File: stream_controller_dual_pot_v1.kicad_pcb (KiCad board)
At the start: 2 copper layers, 46.5 x 48 mm, 36 parts, among them Q1 Q_PMOS_GDS, Q2 Q_PMOS_GDS, SW1 SW_SPDT, U1 MCP1825S, U2 MCP2221AxSL, U3 MCP73831-2-OT, U5 ESP32_WROVER_E, U6 MIC803

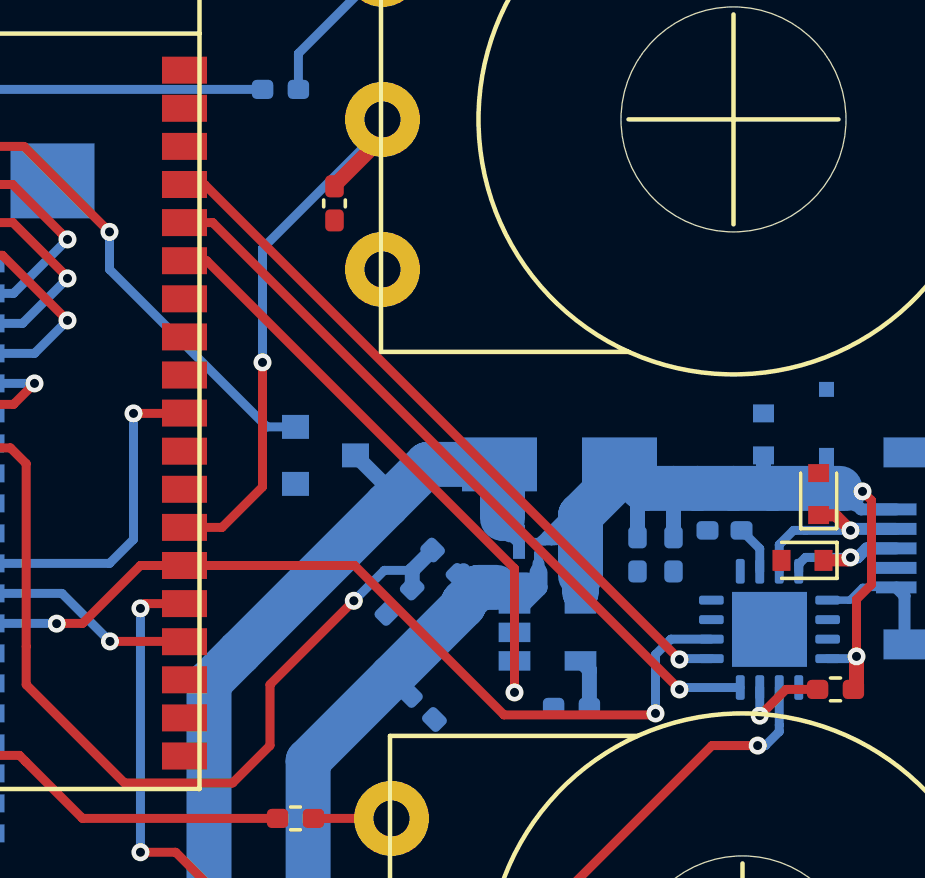
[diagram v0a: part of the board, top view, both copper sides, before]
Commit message: bug UART corrigé
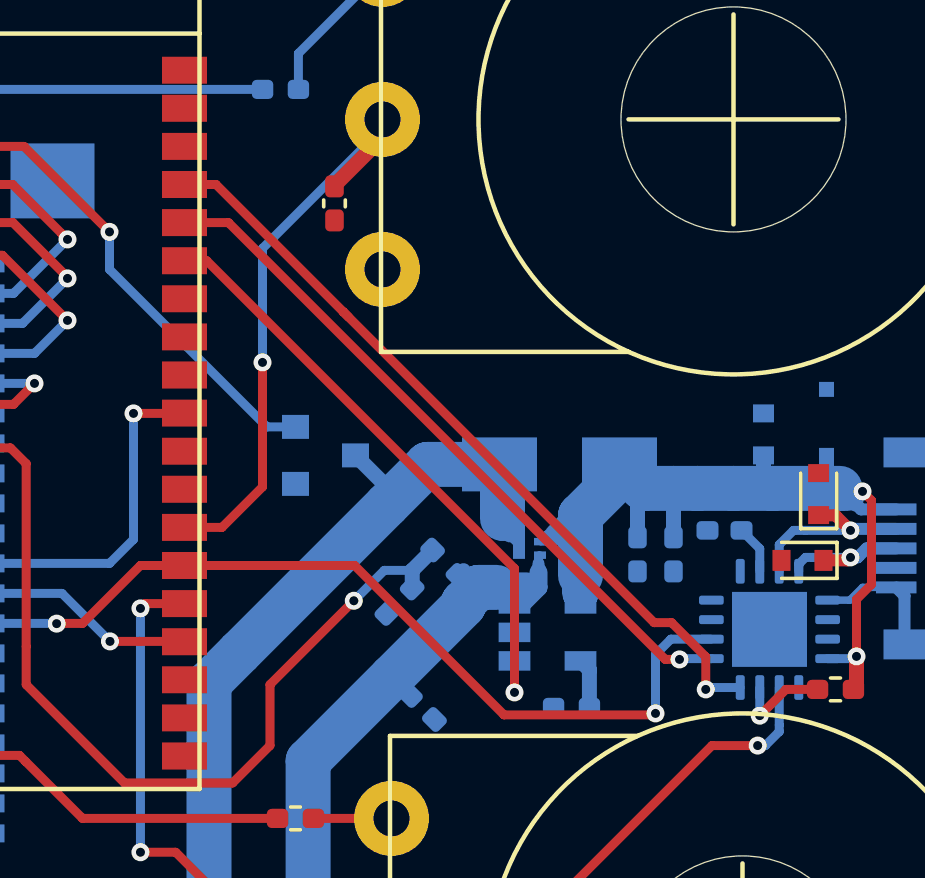
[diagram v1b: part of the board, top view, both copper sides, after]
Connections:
- U2 pad 4: RXD0 -> TXD0
- U2 pad 5: TXD0 -> RXD0
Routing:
- net TXD0: track 24.1 -> 27.1 mm
- net RXD0: track 25.0 -> 23.6 mm

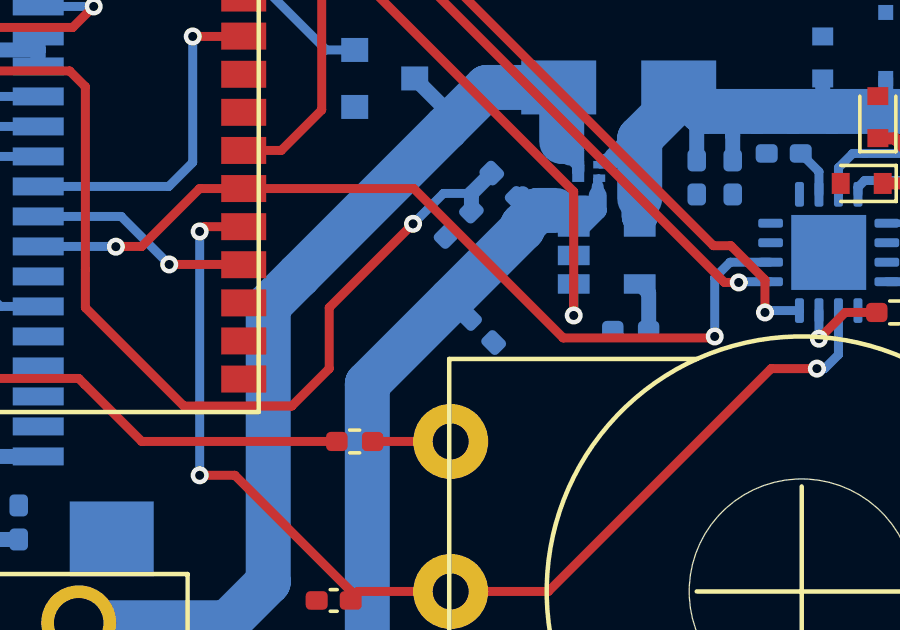
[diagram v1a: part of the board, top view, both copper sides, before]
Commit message: Correction IO0 forcé à 1
Si IO0 n'est pas haut au démarrage, l'ESP32 se met en mode flash. Quand non-connecté par USB, IO0 doit être forcé à 1, car le contrôleur USB n'est pas alimenté.
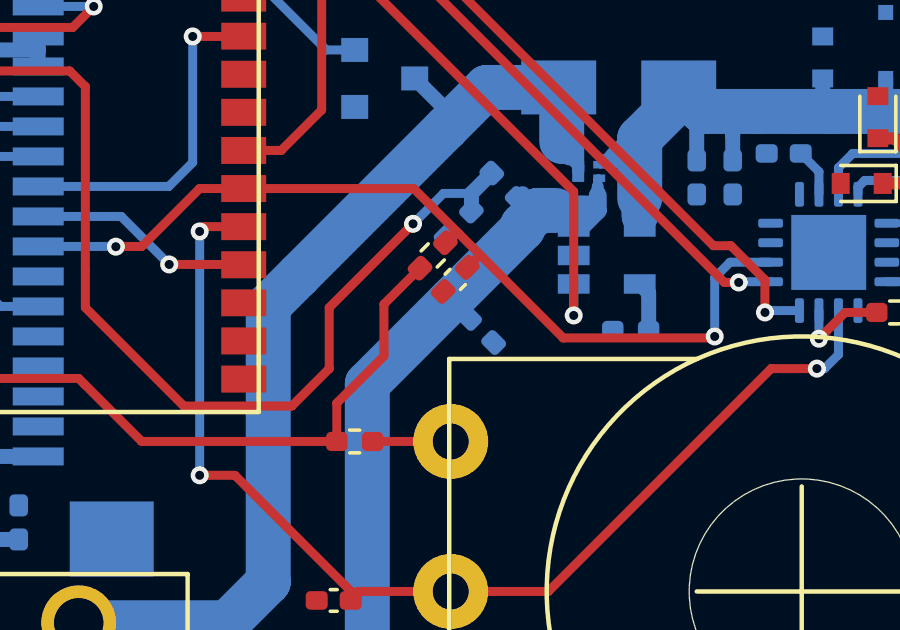
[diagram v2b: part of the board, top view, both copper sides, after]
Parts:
- added C10: 100nF 25V, Capacitor_SMD:C_0402_1005Metric_Pad0.74x0.62mm_HandSolder, F.Cu at (68.0, 33.6)
- added R8: 10k 5%, Resistor_SMD:R_0402_1005Metric_Pad0.72x0.64mm_HandSolder, F.Cu at (67.2, 32.8)
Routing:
- net 3V3: track 88.7 -> 95.6 mm
- net FLASH: track 29.5 -> 30.7 mm

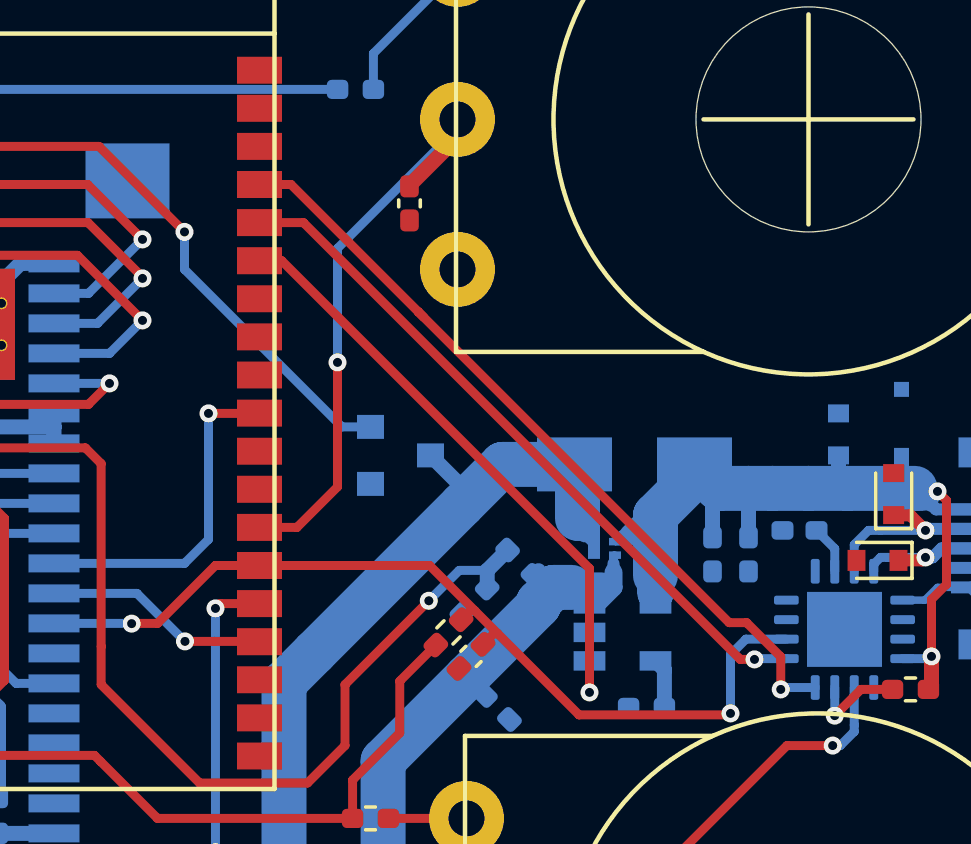
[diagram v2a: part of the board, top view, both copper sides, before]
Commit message: Ajout contrôle pin EN par contrôleur USB
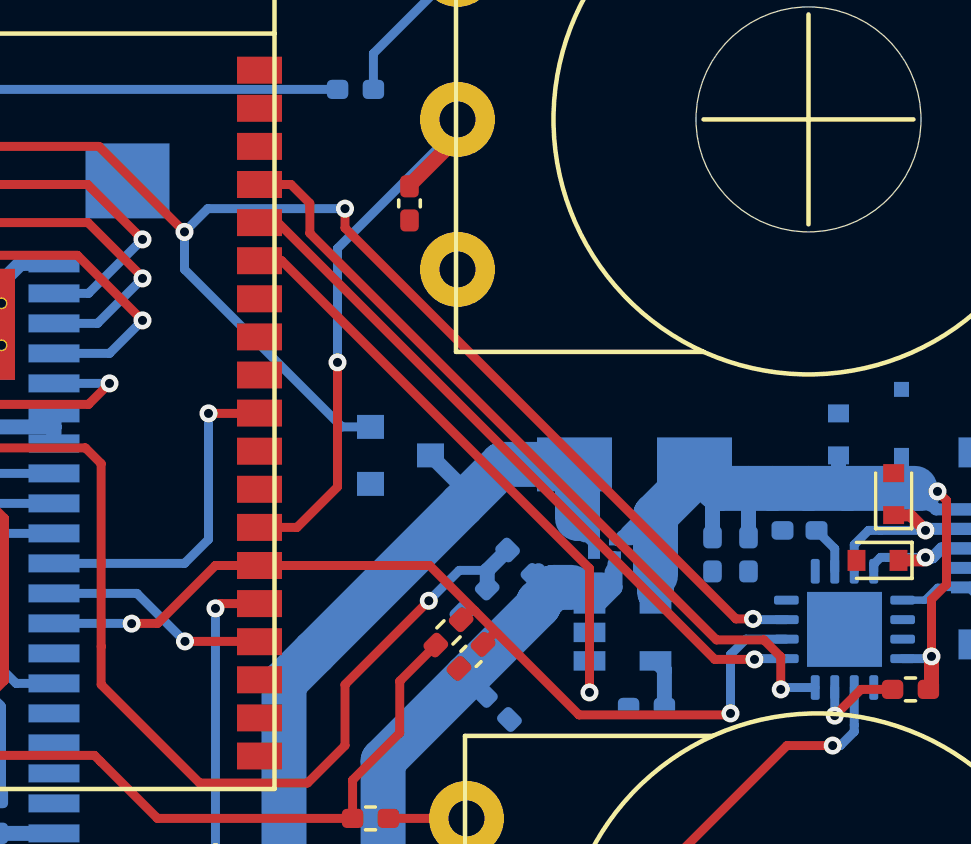
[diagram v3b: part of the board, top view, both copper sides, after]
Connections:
- U2 pad 7: (no net) -> EN
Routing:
- net EN: track 26.0 -> 52.5 mm, vias 2 -> 4
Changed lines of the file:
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@@
     (thickness 1.6)
     (drawings 59)
-    (tracks 394)
+    (tracks 403)
     (zones 0)
     (modules 38)
@@
     (add_net "Net-(D2-Pad1)")
     (add_net "Net-(J_TFT1-Pad20)")
-    (add_net "Net-(J_USB1-Pad4)")
     (add_net "Net-(Q2-Pad3)")
     (add_net "Net-(R1-Pad1)")
@@
     (add_net "Net-(R7-Pad2)")
     (add_net "Net-(SW1-Pad1)")
-    (add_net "Net-(U2-Pad1)")
-    (add_net "Net-(U2-Pad14)")
-    (add_net "Net-(U2-Pad15)")
-    (add_net "Net-(U2-Pad17)")
-    (add_net "Net-(U2-Pad7)")
-    (add_net "Net-(U2-Pad8)")
-    (add_net "Net-(U2-Pad9)")
-    (add_net "Net-(U5-Pad11)")
-    (add_net "Net-(U5-Pad30)")
-    (add_net "Net-(U5-Pad31)")
-    (add_net "Net-(U5-Pad36)")
-    (add_net "Net-(U5-Pad37)")
-    (add_net "Net-(U5-Pad8)")
-    (add_net "Net-(U5-Pad9)")
     (add_net POT1)
     (add_net POT2)
@@
     (pad 9 smd roundrect (at 1.9375 -0.975 90) (size 0.825 0.3) (layers B.Cu B.Paste B.Mask) (roundrect_rratio 0.25))
     (pad 8 smd roundrect (at 0.975 -1.9375 90) (size 0.3 0.825) (layers B.Cu B.Paste B.Mask) (roundrect_rratio 0.25))
-    (pad 7 smd roundrect (at 0.325 -1.9375 90) (size 0.3 0.825) (layers B.Cu B.Paste B.Mask) (roundrect_rratio 0.25))
+    (pad 7 smd roundrect (at 0.325 -1.9375 90) (size 0.3 0.825) (layers B.Cu B.Paste B.Mask) (roundrect_rratio 0.25)
+      (net 20 EN))
     (pad 6 smd roundrect (at -0.325 -1.9375 90) (size 0.3 0.825) (layers B.Cu B.Paste B.Mask) (roundrect_rratio 0.25)
       (net 29 FLASH))
@@
   (segment (start 49.4 16.2975) (end 49.1025 16.2975) (width 0.5) (layer B.Cu) (net 20))
   (segment (start 43.9 16.6) (end 48.8 16.6) (width 0.3) (layer F.Cu) (net 20))
+  (via (at 77.35 32.35) (size 0.6) (drill 0.3) (layers F.Cu B.Cu) (net 20))
+  (segment (start 77.375 32.375) (end 77.35 32.35) (width 0.3) (layer B.Cu) (net 20))
+  (segment (start 78.4625 32.375) (end 77.375 32.375) (width 0.3) (layer B.Cu) (net 20))
+  (via (at 63.75 18.675) (size 0.6) (drill 0.3) (layers F.Cu B.Cu) (net 20))
+  (segment (start 59.175001 18.675) (end 58.4 19.450001) (width 0.3) (layer B.Cu) (net 20))
+  (segment (start 63.75 18.675) (end 59.175001 18.675) (width 0.3) (layer B.Cu) (net 20))
+  (segment (start 63.75 19.318002) (end 63.75 18.675) (width 0.3) (layer F.Cu) (net 20))
+  (segment (start 77.35 32.35) (end 76.781998 32.35) (width 0.3) (layer F.Cu) (net 20))
+  (segment (start 76.781998 32.35) (end 63.75 19.318002) (width 0.3) (layer F.Cu) (net 20))
   (via (at 66.544 31.746) (size 0.6) (drill 0.3) (layers F.Cu B.Cu) (net 21))
   (segment (start 66.544 31.746) (end 63.75 34.54) (width 0.3) (layer F.Cu) (net 21))
@@
   (segment (start 78.3375 34.6375) (end 78.275 34.7) (width 0.3) (layer B.Cu) (net 22))
   (segment (start 79.425 34.6375) (end 78.3375 34.6375) (width 0.3) (layer B.Cu) (net 22))
+  (segment (start 78.275 34.7) (end 78.275 33.612998) (width 0.3) (layer F.Cu) (net 22))
+  (segment (start 78.275 33.612998) (end 77.712001 33.049999) (width 0.3) (layer F.Cu) (net 22))
+  (segment (start 77.712001 33.049999) (end 76.132119 33.049999) (width 0.3) (layer F.Cu) (net 22))
+  (segment (start 76.132119 33.049999) (end 62.57856 19.49644) (width 0.3) (layer F.Cu) (net 22))
   (segment (start 61.95 17.87) (end 60.9 17.87) (width 0.3) (layer F.Cu) (net 22))
-  (segment (start 78.275 33.612998) (end 77.137002 32.475) (width 0.3) (layer F.Cu) (net 22))
-  (segment (start 78.275 34.7) (end 78.275 33.612998) (width 0.3) (layer F.Cu) (net 22))
-  (segment (start 76.555 32.475) (end 66.19 22.11) (width 0.3) (layer F.Cu) (net 22))
-  (segment (start 77.137002 32.475) (end 76.555 32.475) (width 0.3) (layer F.Cu) (net 22))
-  (segment (start 66.19 22.11) (end 61.95 17.87) (width 0.3) (layer F.Cu) (net 22))
-  (segment (start 66.380001 22.300001) (end 66.19 22.11) (width 0.3) (layer F.Cu) (net 22))
+  (segment (start 62.57856 18.49856) (end 61.95 17.87) (width 0.3) (layer F.Cu) (net 22))
+  (segment (start 62.57856 19.49644) (end 62.57856 18.49856) (width 0.3) (layer F.Cu) (net 22))
   (via (at 77.4 33.7) (size 0.6) (drill 0.3) (layers F.Cu B.Cu) (net 23))
   (segment (start 77.425 33.675) (end 77.4 33.7) (width 0.3) (layer B.Cu) (net 23))
   (segment (start 78.4625 33.675) (end 77.425 33.675) (width 0.3) (layer B.Cu) (net 23))
-  (segment (start 76.925 33.7) (end 77.4 33.7) (width 0.3) (layer F.Cu) (net 23))
-  (segment (start 62.365 19.14) (end 76.925 33.7) (width 0.3) (layer F.Cu) (net 23))
-  (segment (start 60.9 19.14) (end 62.365 19.14) (width 0.3) (layer F.Cu) (net 23))
+  (segment (start 61.515 19.14) (end 60.9 19.14) (width 0.3) (layer F.Cu) (net 23))
+  (segment (start 76.075 33.7) (end 61.515 19.14) (width 0.3) (layer F.Cu) (net 23))
+  (segment (start 77.4 33.7) (end 76.075 33.7) (width 0.3) (layer F.Cu) (net 23))
   (via (at 71.9 34.8) (size 0.6) (drill 0.3) (layers F.Cu B.Cu) (net 24))
   (segment (start 71.9 34.8) (end 71.9 33.75) (width 0.3) (layer B.Cu) (net 24))

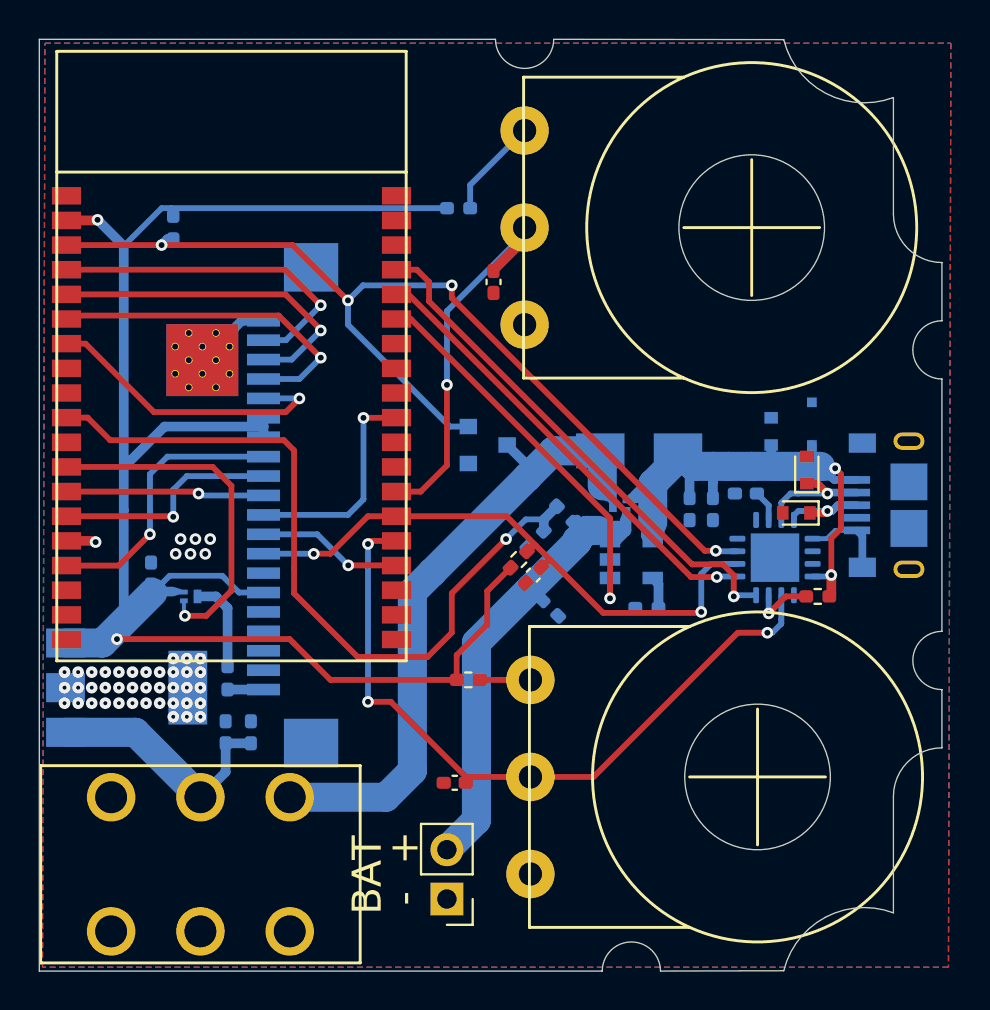
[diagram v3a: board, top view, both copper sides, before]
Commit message: Changements divers
Modifications :
 - toutes les entrées analogiques sur ADC1, car ADC2 ne peut pas être utilisé si le WiFi est actif
 - lecture de l'écran tactile déplacée sur pattes 8, 9, 10 et 11, car les pattes 4, 5, 6 et 7 sont en lecture seule
 - changement du transistor pour le contrôle de la luminosité de l'écran
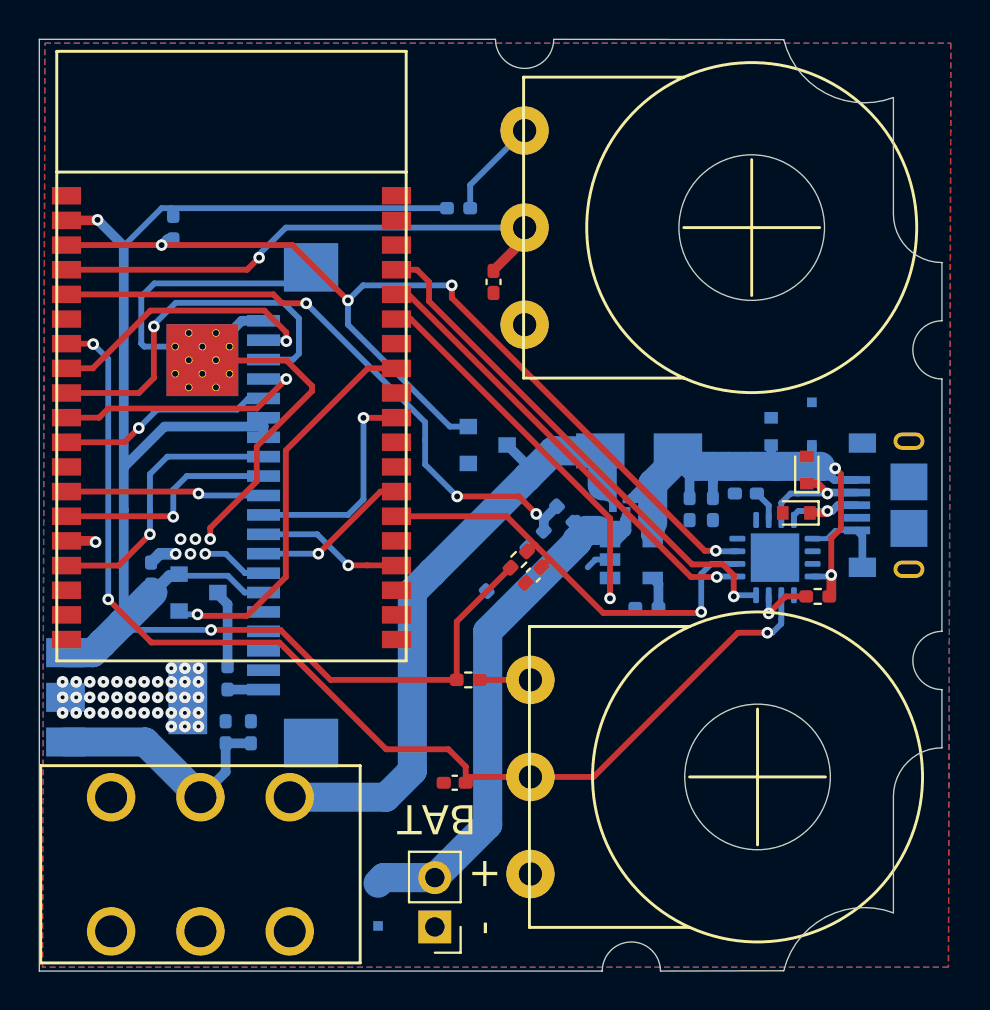
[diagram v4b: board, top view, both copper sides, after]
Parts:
- added D6: 5.42V, Diode_SMD:D_SOD-323F, B.Cu at (60.0, 50.6)
- Q2: footprint Package_DFN_QFN:Diodes_DFN1006-3 -> Package_TO_SOT_SMD:SOT-23
- moved C7 2.92 mm to (66.0, 34.8), turned to 135 degrees
- moved J_BAT1 1.57 mm to (62.9, 51.7)
- moved U1 0.50 mm to (47.0, 39.9)
- moved Q2 0.45 mm to (50.7, 34.5)
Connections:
- J_TFT1 pad 13: FLASH -> TFT_RESET
- J_TFT1 pad NC: (no net) -> GND
- U5 pad 10: VBAT_MON -> TFT_YU
- U5 pad 11: (no net) -> TFT_XR
- U5 pad 12: LED_PWM -> (no net)
- U5 pad 24: POT2 -> (no net)
- U5 pad 26: POT1 -> TFT_RESET
- U5 pad 31: (no net) -> LED_PWM
- U5 pad 4: TFT_YD -> POT1
- U5 pad 5: TFT_XL -> VBAT_MON
- U5 pad 6: TFT_YU -> (no net)
- U5 pad 7: TFT_XR -> POT2
- U5 pad 8: (no net) -> TFT_YD
- U5 pad 9: (no net) -> TFT_XL
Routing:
- net GND: track 11.8 -> 47.8 mm
- net POT2: track 37.9 -> 58.8 mm
- net TFT_RESET: track 0.00 -> 8.18 mm, vias 0 -> 1
- net POT1: track 19.8 -> 27.6 mm
- net FLASH: track 30.7 -> 23.1 mm, vias 2 -> 1
- net VBAT_MON: track 39.7 -> 32.2 mm, vias 1 -> 3
- net TFT_XR: track 15.6 -> 11.1 mm
- net TFT_YU: track 17.5 -> 13.3 mm
- net /VBAT: track 26.0 -> 29.8 mm
- net TFT_YD: track 17.6 -> 14.7 mm
- net 3V3: track 95.6 -> 92.9 mm
- net LED_PWM: track 18.0 -> 20.4 mm
- net TFT_XL: track 17.5 -> 19.6 mm
- net Net-(Q2-Pad3): track 4.80 -> 3.91 mm
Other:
- board text added: "Stream controller dual pot v1.1"
- board text removed: "Stream controller dual pot v1.0"
